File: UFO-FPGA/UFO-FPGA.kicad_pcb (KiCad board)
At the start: 4 copper layers, 68.6 x 53.3 mm, 117 parts, among them J1 Power, J2 Digital, J3 Digital/PWM, J4 Digital, J5 USB_B_Micro, J6 Conn_02x02_Counter_Clockwise, Q1 2N7002, U1 ICE40HX8K-BG121, U11 TL071, U12 MAX11116AUT+T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

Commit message: 0603
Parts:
- R21, R22, R23, R24, R27: footprint Resistor_SMD:R_0805_2012Metric_Pad1.20x1.40mm_HandSolder -> Resistor_SMD:R_0603_1608Metric_Pad0.98x0.95mm_HandSolder

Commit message: pcb
added John zendong
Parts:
- removed TP7: TestPoint, TestPoint:TestPoint_Pad_1.5x1.5mm
- removed U1: ICE40HX8K-BG121, Package_BGA:BGA-121_9.0x9.0mm_Layout11x11_P0.8mm_Ball0.4mm_Pad0.35mm_NSMD
- added G***: LOGO, Graphics:jhon-grap, F.Cu at (167.4, 78.9)
- added TP3: TestPoint, TestPoint:TestPoint_Pad_1.5x1.5mm, F.Cu at (204.0, 112.1)
- added U4: ICE40HX4K-TQ144, Package_QFP:TQFP-144_20x20mm_P0.5mm, F.Cu at (167.0, 79.1)
- D1: moved to F.Cu
- J6: footprint Connector_PinHeader_2.54mm:PinHeader_2x02_P2.54mm_Vertical -> Connector_PinHeader_1.27mm:PinHeader_2x02_P1.27mm_Vertical
- JP1: footprint Connector_PinHeader_2.54mm:PinHeader_1x02_P2.54mm_Vertical -> Connector_PinHeader_1.27mm:PinHeader_1x02_P1.27mm_Vertical
- moved U12 88.5 mm to (257.3, 66.0)
- moved C17 88.5 mm to (244.8, 47.2)
- moved C20 88.5 mm to (261.1, 45.6)
- moved C21 88.5 mm to (252.6, 56.9)
- moved C22 88.5 mm to (252.6, 55.4)
- moved C62 88.5 mm to (251.6, 39.8)
- moved C64 88.5 mm to (255.7, 39.9)
- moved C69 88.5 mm to (247.5, 39.8)
- moved R26 88.5 mm to (257.5, 45.7)
- moved TP5 88.5 mm to (239.1, 40.6)
- moved C15 88.5 mm to (258.4, 54.6)
- moved C16 88.5 mm to (260.4, 54.6)
- moved C18 88.5 mm to (244.6, 45.4)
- moved C19 88.5 mm to (259.4, 45.7)
- moved C23 88.5 mm to (248.5, 38.8)
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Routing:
- net GND: track 149.6 -> 97.3 mm, vias 71 -> 38
- net ICE_SCK: track 45.2 -> 0.00 mm, vias 1 -> 0
- net ICE_SS_B: track 33.2 -> 0.00 mm, vias 1 -> 0
- net +3V3: track 115.4 -> 86.1 mm, vias 33 -> 22
- net ICE_CDONE: track 28.1 -> 0.00 mm, vias 3 -> 0
- net Flash-MOSI: track 25.3 -> 0.00 mm, vias 1 -> 0
- net Flash-MISO: track 24.0 -> 0.00 mm, vias 1 -> 0
- net +1V2: track 32.4 -> 8.75 mm, vias 10 -> 7
- net ICE_CREST: track 24.1 -> 1.47 mm
- net ICE_CLK: track 12.2 -> 0.00 mm
- net /BANK 4 - SPI Programming/ICE_MOSI: track 12.1 -> 0.00 mm, vias 1 -> 0
- net /BANK 4 - SPI Programming/ICE_MISO: track 9.43 -> 0.00 mm
- net /BANK 4 - SPI Programming/N25-CS: track 9.41 -> 0.00 mm, vias 1 -> 0
- net /BANK 4 - SPI Programming/N25-HOLD: track 8.74 -> 0.00 mm
- net /BANK 4 - SPI Programming/VCCPLL1: track 6.23 -> 0.00 mm, vias 2 -> 0
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- removed copper zone on In2.Cu, net +2V5
- removed copper zone on In2.Cu, net /BANK 4 - SPI Programming/VCCPLL0
- removed copper zone on In2.Cu, net /BANK 4 - SPI Programming/VCCPLL1

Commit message: pcb
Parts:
- R5, R6: moved to F.Cu
- moved R6 7.75 mm to (126.8, 67.8), turned to 180 degrees
- moved R5 5.73 mm to (128.8, 71.4)
- moved C7 5.66 mm to (125.9, 72.6), turned to 180 degrees
- moved C10 4.69 mm to (125.9, 70.5), turned to 180 degrees
- moved C11 2.28 mm to (126.8, 65.8)
- moved C12 1.80 mm to (127.0, 64.1)
- moved FB1 0.60 mm to (119.4, 70.5)
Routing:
- net GND: track 97.3 -> 78.6 mm, vias 38 -> 36
- net /USB Programmer/ftd-reset: track 3.68 -> 2.21 mm, vias 1 -> 0
- net +1V8: track 34.3 -> 34.9 mm
- net +5V: track 31.6 -> 32.1 mm
- net /USB Programmer/ftd-ref: track 3.73 -> 3.49 mm, vias 1 -> 0
- net +3V3: track 86.1 -> 86.2 mm, vias 22 -> 21

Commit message: pcb
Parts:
- R22, R24: moved to F.Cu
- U9: footprint Package_SO:SOP-8_3.9x4.9mm_P1.27mm -> Package_SO:SSOP-8_5.25x5.24mm_P1.27mm; moved to F.Cu
- moved R23 38.4 mm to (188.3, 91.0), turned to 180 degrees
- moved R24 5.72 mm to (150.7, 75.5), turned to -90 degrees
- moved R7 4.88 mm to (153.1, 71.0)
- moved C13 4.83 mm to (150.0, 71.7)
- moved U3 4.80 mm to (147.5, 71.8)
- moved U9 3.84 mm to (147.1, 80.3), turned to -90 degrees
- moved R22 2.78 mm to (148.9, 85.8), turned to 180 degrees
- moved TP12 2.73 mm to (142.2, 88.1)
- moved J6 2.31 mm to (151.9, 81.9)
- moved D2 2.02 mm to (140.5, 81.2), turned to 180 degrees
- moved R13 1.06 mm to (138.0, 78.2)
- moved R27 1.06 mm to (139.5, 78.2)
- moved R12 1.06 mm to (136.5, 78.2)
- moved R11 1.04 mm to (135.1, 78.2)
- moved R10 1.04 mm to (133.6, 78.2)
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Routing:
- net ICE_SCK: track 0.00 -> 38.6 mm
- net Flash-MISO: track 0.00 -> 34.0 mm
- net Flash-MOSI: track 0.00 -> 33.3 mm
- net ICE_CDONE: track 0.00 -> 32.1 mm, vias 0 -> 2
- net ICE_SS_B: track 0.00 -> 22.7 mm, vias 0 -> 1
- net /BANK 4 - SPI Programming/N25-CS: track 0.00 -> 16.3 mm, vias 0 -> 1
- net ICE_CREST: track 1.47 -> 12.6 mm, vias 0 -> 2
- net /USB Programmer/FTD-OSCI: track 22.3 -> 14.9 mm
- net +1V8: track 34.9 -> 28.1 mm
- net /BANK 4 - SPI Programming/ICE_MISO: track 0.00 -> 5.13 mm
- net /BANK 4 - SPI Programming/ICE_MOSI: track 0.00 -> 5.07 mm
- net +5V: track 32.1 -> 27.2 mm, vias 11 -> 12
- net +3V3: track 86.2 -> 90.6 mm, vias 21 -> 22
- net /USB Programmer/ICE-SCK: track 0.00 -> 4.05 mm
- net /USB Programmer/ICE-CREST: track 0.00 -> 2.87 mm
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
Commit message: pcb
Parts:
- removed TP3: TestPoint, TestPoint:TestPoint_Pad_1.5x1.5mm
- C16, C21, C22, C29, C30: moved to F.Cu
- moved C15 113.6 mm to (147.9, 81.0), turned to 180 degrees
- moved C16 110.8 mm to (155.1, 89.1), turned to 180 degrees
- moved C22 101.6 mm to (153.1, 75.8), turned to -90 degrees
- moved C21 99.8 mm to (154.6, 75.8), turned to -90 degrees
- moved R25 91.3 mm to (160.3, 78.7), turned to 0 degrees
- moved C23 90.3 mm to (162.6, 66.3), turned to 0 degrees
- moved C18 89.9 mm to (160.3, 76.8), turned to 0 degrees
- moved C17 89.2 mm to (160.1, 75.0), turned to 0 degrees
- moved C24 89.1 mm to (162.6, 64.3), turned to 0 degrees
- moved C29 89.0 mm to (165.5, 93.1)
- moved C30 87.8 mm to (165.5, 91.5)
- moved C69 6.52 mm to (246.1, 33.4)
- moved C61 5.49 mm to (249.7, 34.3)
- moved JP1 1.05 mm to (152.3, 89.9), turned to -90 degrees
- moved R24 0.27 mm to (150.7, 75.8)
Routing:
- net ICE_CREST: track 12.6 -> 29.1 mm
- net +3V3: track 90.6 -> 101.3 mm
- net ICE_SS_B: track 22.7 -> 31.2 mm
- net GND: track 76.8 -> 85.1 mm
- net /BANK 4 - SPI Programming/VCCPLL0: track 0.00 -> 6.82 mm, vias 0 -> 1
- net +1V2: track 6.97 -> 8.69 mm, vias 2 -> 3
- net ICE_SCK: track 38.6 -> 37.0 mm
- net ICE_CDONE: track 32.1 -> 30.8 mm
- net /BANK 4 - SPI Programming/N25-CS: track 16.3 -> 15.2 mm, vias 1 -> 2

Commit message: pcb
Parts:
- removed C57, C58: 100pF, Capacitor_SMD:C_0603_1608Metric_Pad1.08x0.95mm_HandSolder
- removed R52, R53: 510, Resistor_SMD:R_0805_2012Metric
- removed R54: 10, Resistor_SMD:R_0805_2012Metric
- removed U11: TL071, Package_TO_SOT_SMD:SOT-23-5_HandSoldering
- added TP3: TestPoint, TestPoint:TestPoint_Pad_1.0x1.0mm, B.Cu at (156.5, 86.4)
- C15, C17, C20, C31, C32, C61, C67, C69: footprint Capacitor_SMD:C_0603_1608Metric_Pad1.08x0.95mm_HandSolder -> Capacitor_SMD:C_0805_2012Metric_Pad1.18x1.45mm_HandSolder
- C44, C60, C62, C64, R23: moved to F.Cu
- TP1, TP12, TP2, TP5: footprint TestPoint:TestPoint_Pad_1.5x1.5mm -> TestPoint:TestPoint_Pad_1.0x1.0mm
- TP6: footprint TestPoint:TestPoint_Pad_1.5x1.5mm -> TestPoint:TestPoint_Pad_1.0x1.0mm; moved to B.Cu
- moved C64 114.6 mm to (142.6, 58.0), turned to 180 degrees
- moved C44 112.5 mm to (142.4, 56.3), turned to 180 degrees
- moved C62 111.0 mm to (142.7, 61.0), turned to 180 degrees
- moved C60 104.6 mm to (142.7, 59.5), turned to 180 degrees
- moved C61 99.7 mm to (162.5, 82.7), turned to -90 degrees
- moved C69 95.3 mm to (164.5, 82.7), turned to -90 degrees
- moved R26 93.2 mm to (170.5, 79.0)
- moved C19 93.2 mm to (172.4, 79.0)
- moved C20 93.0 mm to (174.4, 79.0)
- moved U12 91.9 mm to (170.0, 94.4)
- moved C31 91.5 mm to (172.4, 82.8)
- moved C32 91.0 mm to (174.4, 82.8)
- moved C43 86.3 mm to (168.5, 82.7), turned to -90 degrees
- moved C67 86.3 mm to (166.5, 82.7), turned to -90 degrees
- moved TP5 85.6 mm to (159.7, 72.5)
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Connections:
- C44 pad 1: +1V2 -> +3V3
- C60 pad 1: +1V2 -> +3V3
- C62 pad 1: +1V2 -> +3V3
- C64 pad 1: +1V2 -> +3V3
- R16 pad 1: RTSn -> /USB Programmer/RTSn-ft
- R17 pad 1: CTSn -> /USB Programmer/CTSn-ft
- R18 pad 2: DTRn -> /USB Programmer/DTRn-ft
- R19 pad 1: DSRn -> /USB Programmer/DSRn-ft
- R20 pad 1: DCDn -> /USB Programmer/DCDn-ft
- U2 pad 40: RTSn -> /USB Programmer/RTSn-ft
- U2 pad 41: CTSn -> /USB Programmer/CTSn-ft
- U2 pad 43: DTRn -> /USB Programmer/DTRn-ft
- U2 pad 44: DSRn -> /USB Programmer/DSRn-ft
- U2 pad 45: DCDn -> /USB Programmer/DCDn-ft
- U4 pad 31: unconnected-(U4D-IOL_24A-Pad31) -> DCDn
- U4 pad 32: unconnected-(U4D-IOL_24B-Pad32) -> DSRn
- U4 pad 33: unconnected-(U4D-IOL_25A-Pad33) -> DTRn
- U4 pad 34: unconnected-(U4D-IOL_25B-Pad34) -> CTSn
- U4 pad 37: unconnected-(U4C-IOB_56-Pad37) -> RTSn
- U4 pad 38: unconnected-(U4C-IOB_57-Pad38) -> RS232_Tx_TTL
- U4 pad 39: unconnected-(U4C-IOB_61-Pad39) -> RS232_Rx_TTL
- U4 pad 52: unconnected-(U4C-IOB_82_GBIN4-Pad52) -> ICE_CLK
- U4 pad 96: unconnected-(U4B-IOR_146-Pad96) -> SCK
- U4 pad 97: unconnected-(U4B-IOR_147-Pad97) -> MISO
- U4 pad 98: unconnected-(U4B-IOR_148-Pad98) -> ADC-CS
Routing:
- net +3V3: track 101.3 -> 132.8 mm, vias 22 -> 29
- net GND: track 85.1 -> 113.9 mm, vias 36 -> 44
- net +1V2: track 8.69 -> 30.1 mm, vias 3 -> 10
- net DCDn: track 0.00 -> 17.0 mm
- net DSRn: track 0.00 -> 15.5 mm
- net DTRn: track 0.00 -> 14.0 mm
- net ICE_CLK: track 0.00 -> 13.7 mm, vias 0 -> 2
- net CTSn: track 0.00 -> 12.6 mm
- net /USB Programmer/DCDn-ft: track 0.00 -> 10.3 mm
- net /USB Programmer/DSRn-ft: track 0.00 -> 9.76 mm
- net /BANK 4 - SPI Programming/VCCPLL1: track 0.00 -> 9.62 mm, vias 0 -> 1
- net RTSn: track 0.00 -> 9.17 mm
- net /USB Programmer/DTRn-ft: track 0.00 -> 9.07 mm
- net /USB Programmer/CTSn-ft: track 0.00 -> 8.75 mm
- net RS232_Tx_TTL: track 0.00 -> 8.75 mm
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
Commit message: pcb
added monkey
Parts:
- added G***: LOGO, Graphics:monkey 2, F.Cu at (136.7, 69.7)
- moved C13 1.20 mm to (148.3, 73.3)
- moved R14 0.87 mm to (148.9, 69.2)
- moved R15 0.84 mm to (148.9, 67.6)
- moved R16 0.80 mm to (148.9, 66.1)
- moved R17 0.79 mm to (148.9, 64.5)
- moved R18 0.78 mm to (148.9, 63.0)
- moved R20 0.77 mm to (148.9, 59.9)
- moved R19 0.76 mm to (148.9, 61.5)
- moved R7 0.62 mm to (148.2, 71.2)
- moved U12 0.40 mm to (170.2, 94.1)
- moved D1 0.31 mm to (173.9, 91.8)
- moved C29 0.17 mm to (165.7, 93.1)
- moved C30 0.17 mm to (165.7, 91.5)
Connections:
- J1 pad 1: PIN-22 -> PIN-25
- J1 pad 2: PIN-23 -> PIN-24
- J1 pad 3: PIN-24 -> PIN-23
- J1 pad 8: GND -> unconnected-(J1-Pin_8-Pad8)
- J2 pad 1: PIN-18 -> PIN-22
- J2 pad 2: PIN-19 -> PIN-21
- J2 pad 4: PIN-21 -> PIN-19
- J2 pad 5: GND -> PIN-18
- U4 pad 10: unconnected-(U4D-IOL_5B-Pad10) -> PIN-12
- U4 pad 11: unconnected-(U4D-IOL_8A-Pad11) -> PIN-11
- U4 pad 12: unconnected-(U4D-IOL_8B-Pad12) -> PIN-10
- U4 pad 15: unconnected-(U4D-IOL_10A-Pad15) -> PIN-9
- U4 pad 16: unconnected-(U4D-IOL_10B-Pad16) -> PIN-8
- U4 pad 17: unconnected-(U4D-IOL_12A-Pad17) -> PIN-7
- U4 pad 18: unconnected-(U4D-IOL_12B-Pad18) -> PIN-6
- U4 pad 19: unconnected-(U4D-IOL_13A-Pad19) -> PIN-5
- U4 pad 20: unconnected-(U4D-IOL_13B_GBIN7-Pad20) -> PIN-4
- U4 pad 21: unconnected-(U4D-IOL_14A_GBIN6-Pad21) -> PIN-3
- U4 pad 22: unconnected-(U4D-IOL_14B-Pad22) -> PIN-2
- U4 pad 23: unconnected-(U4D-IOL_17A-Pad23) -> PIN-1
- U4 pad 3: unconnected-(U4D-IOL_3A-Pad3) -> PIN-17
- U4 pad 4: unconnected-(U4D-IOL_3B-Pad4) -> PIN-16
- U4 pad 7: unconnected-(U4D-IOL_4A-Pad7) -> PIN-15
- U4 pad 73: unconnected-(U4B-IOR_109-Pad73) -> PIN-25
- U4 pad 74: unconnected-(U4B-IOR_110-Pad74) -> PIN-24
- U4 pad 75: unconnected-(U4B-IOR_111-Pad75) -> PIN-23
- U4 pad 76: unconnected-(U4B-IOR_112-Pad76) -> PIN-22
- U4 pad 78: unconnected-(U4B-IOR_114-Pad78) -> PIN-21
- U4 pad 79: unconnected-(U4B-IOR_115-Pad79) -> PIN-20
- U4 pad 8: unconnected-(U4D-IOL_4B-Pad8) -> PIN-14
- U4 pad 80: unconnected-(U4B-IOR_116-Pad80) -> PIN-19
- U4 pad 81: unconnected-(U4B-IOR_117-Pad81) -> PIN-18
- U4 pad 9: unconnected-(U4D-IOL_5A-Pad9) -> PIN-13
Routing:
- net PIN-1: track 0.00 -> 46.1 mm, vias 0 -> 1
- net PIN-2: track 0.00 -> 43.7 mm
- net PIN-3: track 0.00 -> 43.6 mm, vias 0 -> 1
- net PIN-5: track 0.00 -> 36.7 mm, vias 0 -> 1
- net PIN-4: track 0.00 -> 35.8 mm
- net PIN-7: track 0.00 -> 33.9 mm, vias 0 -> 1
- net PIN-6: track 0.00 -> 32.3 mm
- net PIN-8: track 0.00 -> 29.4 mm
- net PIN-9: track 0.00 -> 28.3 mm
- net PIN-10: track 0.00 -> 25.1 mm, vias 0 -> 1
- net PIN-25: track 0.00 -> 23.2 mm
- net PIN-11: track 0.00 -> 23.1 mm
- net PIN-12: track 0.00 -> 21.5 mm
- net PIN-24: track 0.00 -> 21.5 mm
- net PIN-13: track 0.00 -> 20.7 mm
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
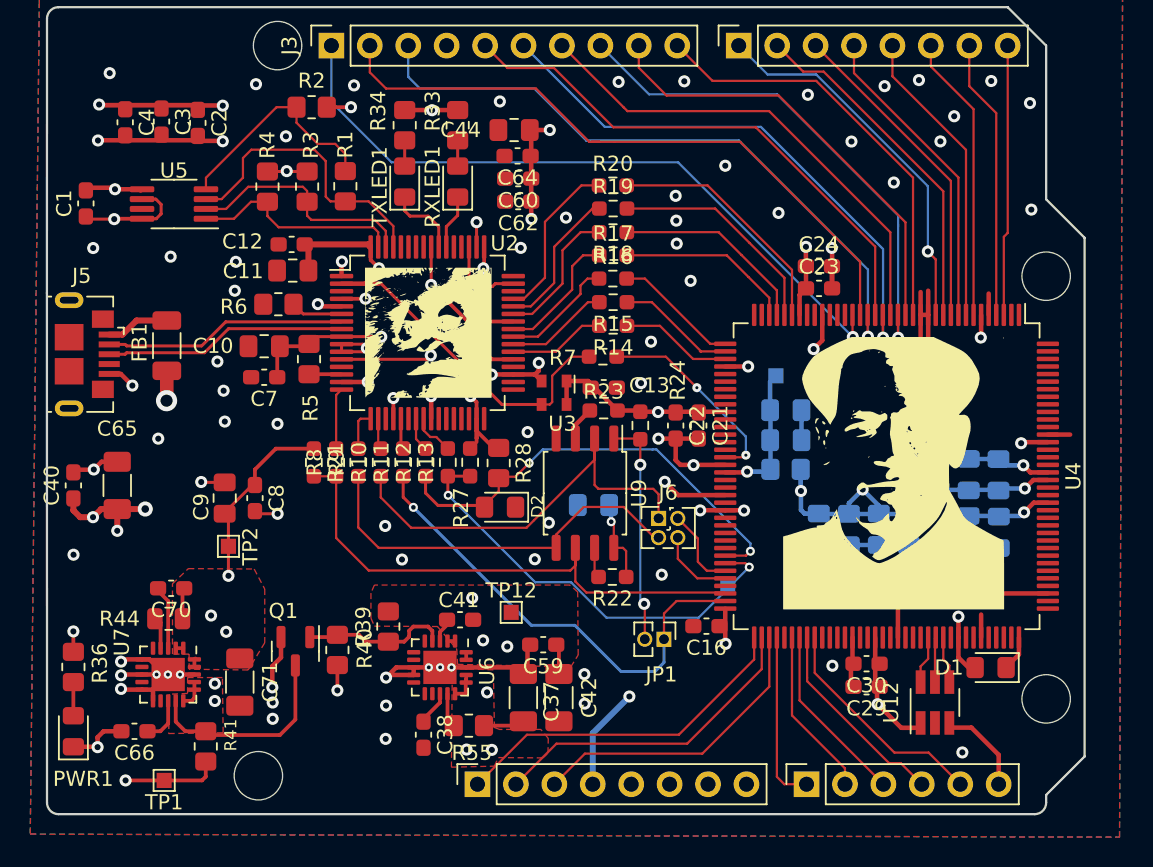
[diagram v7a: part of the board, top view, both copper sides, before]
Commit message: vias and silkscreen
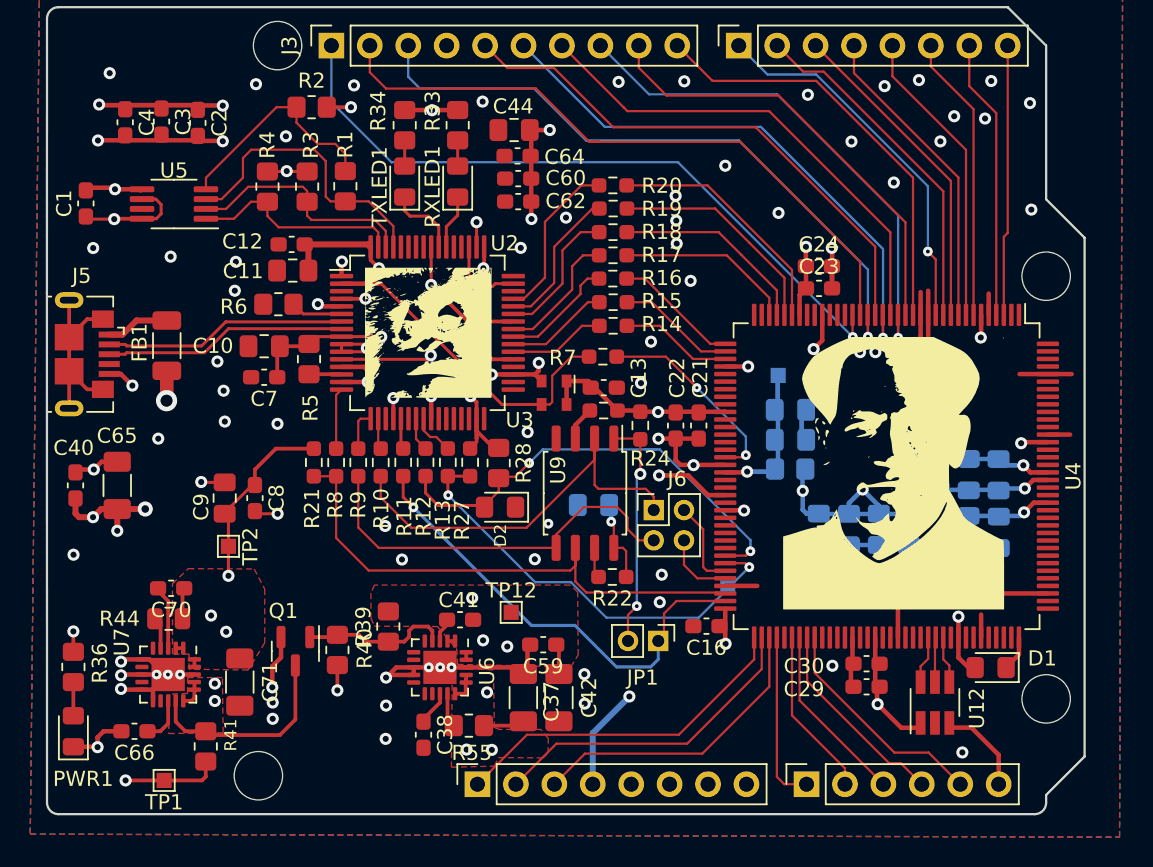
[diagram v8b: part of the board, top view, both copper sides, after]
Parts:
- J6: footprint Connector_PinHeader_1.27mm:PinHeader_2x02_P1.27mm_Vertical -> Connector_PinHeader_2.00mm:PinHeader_2x02_P2.00mm_Vertical
- JP1: footprint Connector_PinHeader_1.27mm:PinHeader_1x02_P1.27mm_Vertical -> Connector_PinHeader_2.00mm:PinHeader_1x02_P2.00mm_Vertical
- moved J6 0.64 mm to (151.6, 81.4)
- moved JP1 0.39 mm to (151.9, 90.0)
- moved C17 0.31 mm to (160.6, 74.8)
- moved C18 0.31 mm to (160.7, 76.7)
- moved R25 0.31 mm to (160.6, 78.7)
- moved TP5 0.14 mm to (159.8, 72.5), turned to 180 degrees
- moved C40 0.14 mm to (113.4, 79.8)
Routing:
- net unconnected-(J5-Shield-Pad6): track 0.00 -> 12.6 mm
- net GND: track 120.0 -> 126.6 mm, vias 84 -> 88
- net Flash-MISO: track 29.2 -> 28.2 mm
- net ICE_SS_B: track 31.3 -> 30.4 mm
- net ICE_CDONE: track 29.9 -> 30.7 mm
- net /BANK 4 - SPI Programming/VCCPLL0: track 9.25 -> 8.57 mm
- net PIN-19: track 13.9 -> 13.3 mm
